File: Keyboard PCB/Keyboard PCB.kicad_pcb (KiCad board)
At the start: 2 copper layers, 3.6 x 3.3 mm, 9 parts, among them SW1 SW_Push, SW2 SW_Push, SW3 SW_Push, SW4 SW_Push, SW5 SW_Push, SW6 SW_Push, U1 MOUDLE-SEEEDUINO-XIAO

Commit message: Updated PCB
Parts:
- D1, D2: value SK6812MINI-E -> SK6812MINI; footprint footprints:SK6812MINI-E_fixed -> LED_SMD:LED_SK6812MINI_PLCC4_3.5x3.5mm_P1.75mm
- moved D2 38.7 mm to (32.7, 58.7)
- moved D1 37.5 mm to (70.8, 58.7)
- moved SW5 4.76 mm to (102.6, 54.5)
- moved SW6 4.76 mm to (102.6, 73.5)
- moved U1 3.62 mm to (76.2, 45.2)
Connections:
- D1 pad 1: +5V -> Net-(D1-DOUT)
- D1 pad 2: (no net) -> GND
- D1 pad 3: GND -> Net-(D1-DIN)
- D1 pad 4: Net-(D1-DIN) -> +5V
- D2 pad 1: +5V -> unconnected-(D2-DOUT-Pad1)
- D2 pad 2: (no net) -> GND
- D2 pad 3: GND -> Net-(D1-DOUT)
- D2 pad 4: Net-(D1-DOUT) -> +5V
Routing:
- net GND: track 0.00 -> 172.5 mm
- net Net-(U1-PA6_A10_D10_MOSI): track 0.00 -> 74.7 mm
- net Net-(U1-PA9_A5_D5_SCL): track 0.00 -> 42.3 mm
- net Net-(D1-DOUT): track 0.00 -> 39.3 mm
- net +5V: track 0.00 -> 39.2 mm
- net Net-(U1-PA5_A9_D9_MISO): track 0.00 -> 34.3 mm
- net Net-(U1-PB09_A7_D7_RX): track 0.00 -> 27.4 mm
- net Net-(D1-DIN): track 0.00 -> 20.7 mm
- net Net-(U1-PB08_A6_D6_TX): track 0.00 -> 19.4 mm
- net Net-(U1-PA7_A8_D8_SCK): track 0.00 -> 15.4 mm
- net unconnected-(U1-5V-Pad14): track 0.00 -> 0.64 mm
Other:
- board outline removed

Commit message: Who needs autosaves?
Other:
- board outline added: 85.7 x 53.4 mm
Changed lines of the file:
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@@
 		(embedded_fonts no)
+	)
+	(gr_rect
+		(start 23.8125 34.71875)
+		(end 109.5375 88.10625)
+		(stroke
+			(width 0.05)
+			(type default)
+		)
+		(fill no)
+		(layer "Edge.Cuts")
 	)
 	(segment

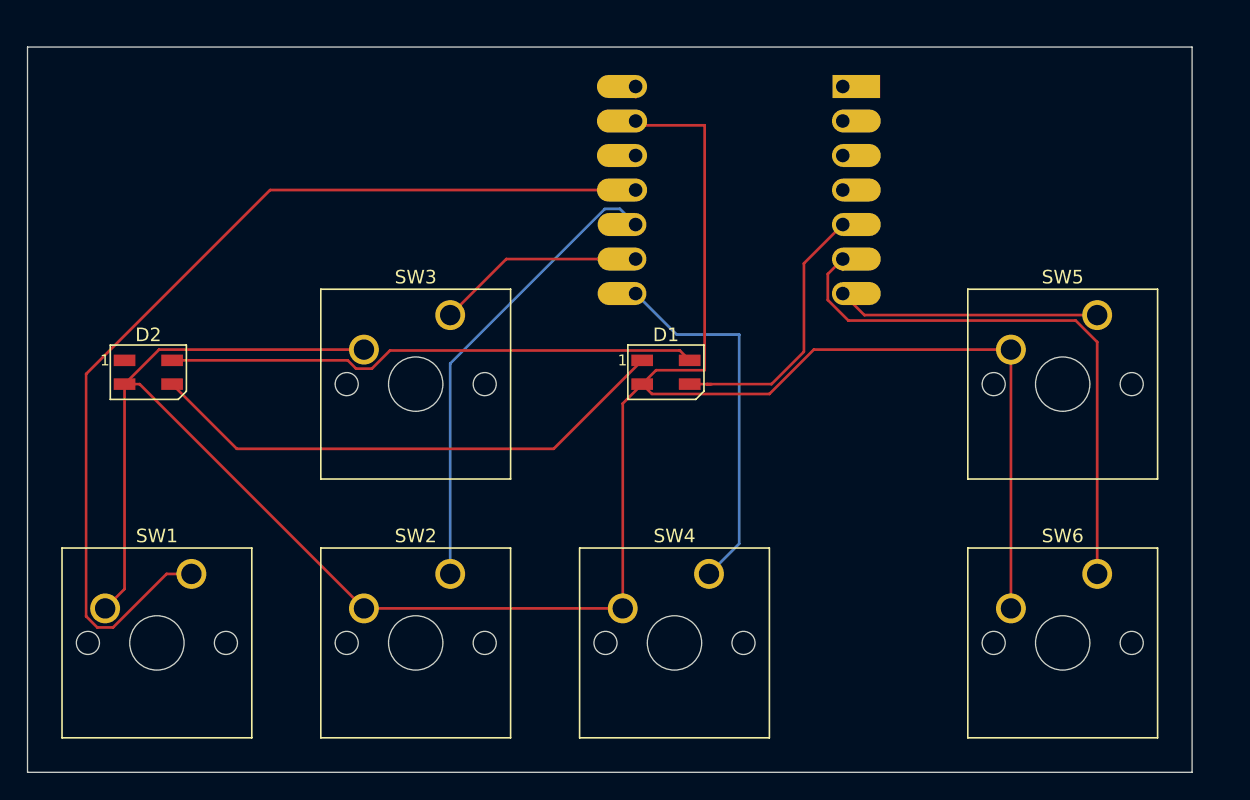
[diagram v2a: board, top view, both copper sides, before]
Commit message: Adjusted wiring
I flipped the XIAO microcontroller because I was worried it would mess up the build process if it was on the bottom. For some reason the tutorial says to put it on the back side but most people just put it on top.
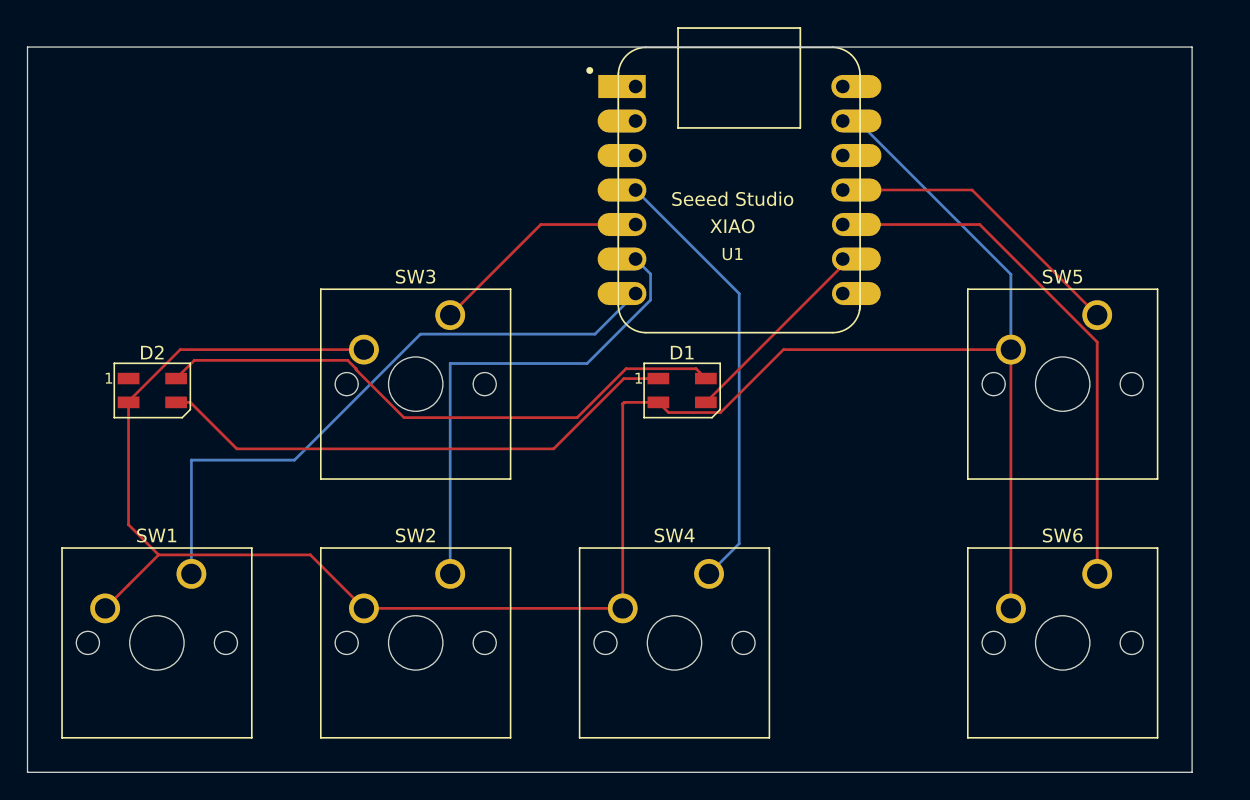
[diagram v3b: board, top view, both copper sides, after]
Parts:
- U1: moved to F.Cu
- moved D1 1.80 mm to (72.0, 60.0)
- moved D2 1.38 mm to (33.0, 60.0)
- turned U1 to 0 degrees
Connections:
- SW1 pad 1: Net-(U1-PA6_A10_D10_MOSI) -> Net-(U1-PB08_A6_D6_TX)
- SW2 pad 1: Net-(U1-PA5_A9_D9_MISO) -> Net-(U1-PA9_A5_D5_SCL)
- SW3 pad 1: Net-(U1-PA7_A8_D8_SCK) -> Net-(U1-PA8_A4_D4_SDA)
- SW4 pad 1: Net-(U1-PB09_A7_D7_RX) -> Net-(U1-PA11_A3_D3)
- SW5 pad 1: Net-(U1-PB08_A6_D6_TX) -> Net-(U1-PA6_A10_D10_MOSI)
- SW6 pad 1: Net-(U1-PA9_A5_D5_SCL) -> Net-(U1-PA5_A9_D9_MISO)
- U1 pad 4: unconnected-(U1-PA11_A3_D3-Pad4) -> Net-(U1-PA11_A3_D3)
- U1 pad 5: Net-(D1-DIN) -> Net-(U1-PA8_A4_D4_SDA)
- U1 pad 8: Net-(U1-PB09_A7_D7_RX) -> unconnected-(U1-PB09_A7_D7_RX-Pad8)
- U1 pad 9: Net-(U1-PA7_A8_D8_SCK) -> Net-(D1-DIN)
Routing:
- net Net-(U1-PA6_A10_D10_MOSI): track 74.7 -> 22.5 mm
- net Net-(U1-PA11_A3_D3): track 0.00 -> 32.3 mm
- net Net-(U1-PB09_A7_D7_RX): track 27.4 -> 0.00 mm
- net Net-(U1-PB08_A6_D6_TX): track 19.4 -> 46.2 mm
- net Net-(U1-PA8_A4_D4_SDA): track 0.00 -> 16.4 mm
- net Net-(U1-PA7_A8_D8_SCK): track 15.4 -> 0.00 mm
- net GND: track 172.5 -> 160.1 mm
- net Net-(U1-PA9_A5_D5_SCL): track 42.3 -> 35.6 mm
- net Net-(D1-DIN): track 20.7 -> 14.7 mm
- net Net-(U1-PA5_A9_D9_MISO): track 34.3 -> 39.4 mm
- net +5V: track 39.2 -> 43.1 mm
- net unconnected-(U1-5V-Pad14): track 0.64 -> 0.00 mm
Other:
- board text added: "D1"
